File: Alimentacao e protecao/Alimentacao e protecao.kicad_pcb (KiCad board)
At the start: 2 copper layers, 18 parts, among them J1 PinoCheckBateriaVcc, J2 PinoCheckBateriaGND, J3 Conn_01x01_MedidorBateriaVcc, J4 Conn_01x01_MedidorBateriaGnd, Q1 BC548, Q2 BC548, SW1 SW_ON/OFF

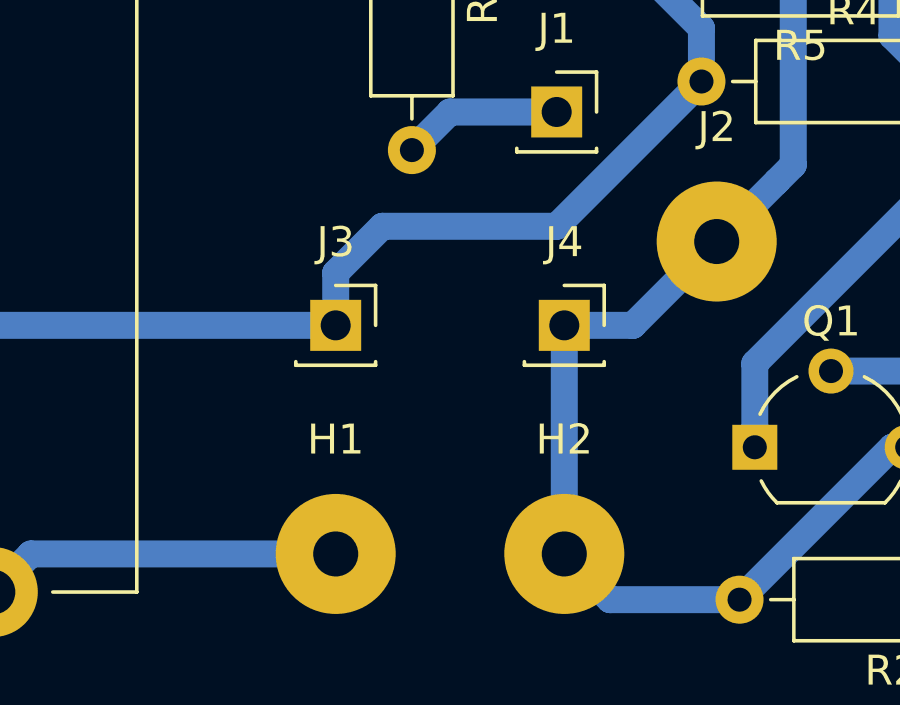
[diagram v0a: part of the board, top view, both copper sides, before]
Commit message: Distribuição dos compenentes praticamente concluída, quase pronta para root.
Placa Central: 5VArduino(pino 15) colocado no pino 16, enquanto o sensorEsq(pino 16) foi colocado no pino 15 para
facilitar o root; Adicionado na placa central os pads de conexao das alimentacoes provenientes do circuito de
alimentacao; Label '5V' substituída por '5VArduino' - decisão a ser revisada; Pads de solda trocados por pads maiores
por questoes de corrente alta (pinos de alimentacao). *Placa de Alimentação: Nome de dois pinos da placa de alimentação
modificados. Pads de solda trocados por pads maiores por questoes de corrente alta (pinos de alimentacao).
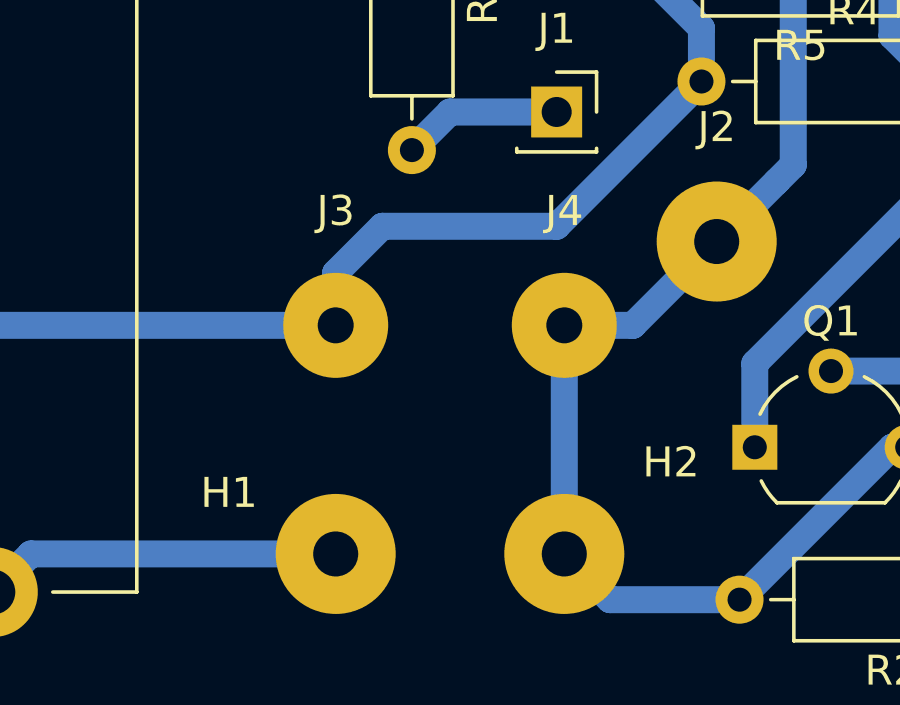
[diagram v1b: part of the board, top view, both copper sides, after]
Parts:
- J3: value Conn_01x01_MedidorBateriaVcc -> 8.4V_PlacaCentral; footprint Connector_PinSocket_2.54mm:PinSocket_1x01_P2.54mm_Vertical -> Connector_Wire:SolderWirePad_1x01_Drill1.2mm
- J4: value Conn_01x01_MedidorBateriaGnd -> GND_PlacaCentral; footprint Connector_PinSocket_2.54mm:PinSocket_1x01_P2.54mm_Vertical -> Connector_Wire:SolderWirePad_1x01_Drill1.2mm
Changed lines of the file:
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@@
       (effects (font (size 1 1) (thickness 0.15)))
     )
-    (fp_text value Fuse-5A (at 13 6 90) (layer F.Fab)
+    (fp_text value Fuse-5A (at 18.034 6 90) (layer F.Fab)
       (effects (font (size 1 1) (thickness 0.15)))
     )
@@
     (tags connector)
     (attr virtual)
-    (fp_text reference H1 (at 0 -3.81) (layer F.SilkS)
+    (fp_text reference H1 (at -3.556 -2.032) (layer F.SilkS)
       (effects (font (size 1 1) (thickness 0.15)))
     )
@@
     (tags connector)
     (attr virtual)
-    (fp_text reference H2 (at 0 -3.81) (layer F.SilkS)
+    (fp_text reference H2 (at 3.556 -3.048) (layer F.SilkS)
       (effects (font (size 1 1) (thickness 0.15)))
     )
@@
       (effects (font (size 1 1) (thickness 0.15)))
     )
-    (fp_text value PinoCheckBateriaGND (at 0 3.81) (layer F.Fab)
+    (fp_text value PinoCheckBateriaGND (at 10.922 -0.508) (layer F.Fab)
       (effects (font (size 1 1) (thickness 0.15)))
     )
@@
     (pad 1 thru_hole circle (at 0 0) (size 4.0005 4.0005) (drill 1.50114) (layers *.Cu *.Mask)
       (net 8 GND))
-  )
-  (module Connector_PinSocket_2.54mm:PinSocket_1x01_P2.54mm_Vertical (layer F.Cu)
-    (at 76.2 90.17)
-    (descr "Through hole straight socket strip, 1x01, 2.54mm pitch, single row (from Kicad 4.0.7), script generated")
-    (tags "Through hole socket strip THT 1x01 2.54mm single row")
-    (fp_text reference J3 (at 0 -2.77) (layer F.SilkS)
-      (effects (font (size 1 1) (thickness 0.15)))
-    )
-    (fp_text value Conn_01x01_MedidorBateriaVcc (at 0 2.77) (layer F.Fab)
-      (effects (font (size 1 1) (thickness 0.15)))
-    )
-    (fp_text user %R (at 0 0) (layer F.Fab)
-      (effects (font (size 1 1) (thickness 0.15)))
-    )
-    (fp_line (start -1.8 1.75) (end -1.8 -1.8) (layer F.CrtYd) (width 0.05))
-    (fp_line (start 1.75 1.75) (end -1.8 1.75) (layer F.CrtYd) (width 0.05))
-    (fp_line (start 1.75 -1.8) (end 1.75 1.75) (layer F.CrtYd) (width 0.05))
-    (fp_line (start -1.8 -1.8) (end 1.75 -1.8) (layer F.CrtYd) (width 0.05))
-    (fp_line (start 0 -1.33) (end 1.33 -1.33) (layer F.SilkS) (width 0.12))
-    (fp_line (start 1.33 -1.33) (end 1.33 0) (layer F.SilkS) (width 0.12))
-    (fp_line (start 1.33 1.21) (end 1.33 1.33) (layer F.SilkS) (width 0.12))
-    (fp_line (start -1.33 1.21) (end -1.33 1.33) (layer F.SilkS) (width 0.12))
-    (fp_line (start -1.33 1.33) (end 1.33 1.33) (layer F.SilkS) (width 0.12))
-    (fp_line (start -1.27 1.27) (end -1.27 -1.27) (layer F.Fab) (width 0.1))
-    (fp_line (start 1.27 1.27) (end -1.27 1.27) (layer F.Fab) (width 0.1))
-    (fp_line (start 1.27 -0.635) (end 1.27 1.27) (layer F.Fab) (width 0.1))
-    (fp_line (start 0.635 -1.27) (end 1.27 -0.635) (layer F.Fab) (width 0.1))
-    (fp_line (start -1.27 -1.27) (end 0.635 -1.27) (layer F.Fab) (width 0.1))
-    (pad 1 thru_hole rect (at 0 0) (size 1.7 1.7) (drill 1) (layers *.Cu *.Mask)
-      (net 3 8.4V))
-    (model ${KISYS3DMOD}/Connector_PinSocket_2.54mm.3dshapes/PinSocket_1x01_P2.54mm_Vertical.wrl
-      (at (xyz 0 0 0))
-      (scale (xyz 1 1 1))
-      (rotate (xyz 0 0 0))
-    )
-  )
-  (module Connector_PinSocket_2.54mm:PinSocket_1x01_P2.54mm_Vertical (layer F.Cu)
-    (at 83.82 90.17)
-    (descr "Through hole straight socket strip, 1x01, 2.54mm pitch, single row (from Kicad 4.0.7), script generated")
-    (tags "Through hole socket strip THT 1x01 2.54mm single row")
-    (fp_text reference J4 (at 0 -2.77) (layer F.SilkS)
-      (effects (font (size 1 1) (thickness 0.15)))
-    )
-    (fp_text value Conn_01x01_MedidorBateriaGnd (at 0 2.77) (layer F.Fab)
-      (effects (font (size 1 1) (thickness 0.15)))
-    )
-    (fp_line (start -1.27 -1.27) (end 0.635 -1.27) (layer F.Fab) (width 0.1))
-    (fp_line (start 0.635 -1.27) (end 1.27 -0.635) (layer F.Fab) (width 0.1))
-    (fp_line (start 1.27 -0.635) (end 1.27 1.27) (layer F.Fab) (width 0.1))
-    (fp_line (start 1.27 1.27) (end -1.27 1.27) (layer F.Fab) (width 0.1))
-    (fp_line (start -1.27 1.27) (end -1.27 -1.27) (layer F.Fab) (width 0.1))
-    (fp_line (start -1.33 1.33) (end 1.33 1.33) (layer F.SilkS) (width 0.12))
-    (fp_line (start -1.33 1.21) (end -1.33 1.33) (layer F.SilkS) (width 0.12))
-    (fp_line (start 1.33 1.21) (end 1.33 1.33) (layer F.SilkS) (width 0.12))
-    (fp_line (start 1.33 -1.33) (end 1.33 0) (layer F.SilkS) (width 0.12))
-    (fp_line (start 0 -1.33) (end 1.33 -1.33) (layer F.SilkS) (width 0.12))
-    (fp_line (start -1.8 -1.8) (end 1.75 -1.8) (layer F.CrtYd) (width 0.05))
-    (fp_line (start 1.75 -1.8) (end 1.75 1.75) (layer F.CrtYd) (width 0.05))
-    (fp_line (start 1.75 1.75) (end -1.8 1.75) (layer F.CrtYd) (width 0.05))
-    (fp_line (start -1.8 1.75) (end -1.8 -1.8) (layer F.CrtYd) (width 0.05))
-    (fp_text user %R (at 0 0) (layer F.Fab)
-      (effects (font (size 1 1) (thickness 0.15)))
-    )
-    (pad 1 thru_hole rect (at 0 0) (size 1.7 1.7) (drill 1) (layers *.Cu *.Mask)
-      (net 8 GND))
-    (model ${KISYS3DMOD}/Connector_PinSocket_2.54mm.3dshapes/PinSocket_1x01_P2.54mm_Vertical.wrl
-      (at (xyz 0 0 0))
-      (scale (xyz 1 1 1))
-      (rotate (xyz 0 0 0))
-    )
   )
   (module Package_TO_SOT_THT:TO-92_Wide (layer F.Cu)
@@
       (effects (font (size 1 1) (thickness 0.15)))
     )
-    (fp_text value R6K6MedidorDeBateria (at 5.08 2.37 180) (layer F.Fab)
+    (fp_text value R6K6MedidorDeBateria (at -7.874 -3.302 180) (layer F.Fab)
       (effects (font (size 1 1) (thickness 0.15)))
     )
@@
       (effects (font (size 1 1) (thickness 0.15)))
     )
-    (fp_text value R1KMedidorDeBateria (at 5.08 2.37 90) (layer F.Fab)
+    (fp_text value R1KMedidorDeBateria (at 0.254 12.7 180) (layer F.Fab)
       (effects (font (size 1 1) (thickness 0.15)))
     )
@@
       (effects (font (size 1 1) (thickness 0.15)))
     )
-    (fp_text value SW_ON/OFF (at 0 -0.5 90) (layer F.Fab)
+    (fp_text value SW_ON/OFF (at 0.762 -6.858 90) (layer F.Fab)
       (effects (font (size 1 1) (thickness 0.15)))
     )
@@
       (net 3 8.4V))
   )
+  (module Connector_Wire:SolderWirePad_1x01_Drill1.2mm (layer F.Cu)
+    (at 76.2 90.17)
+    (descr "Wire solder connection")
+    (tags connector)
+    (attr virtual)
+    (fp_text reference J3 (at 0 -3.81) (layer F.SilkS)
+      (effects (font (size 1 1) (thickness 0.15)))
+    )
+    (fp_text value 8.4V_PlacaCentral (at 0 3.175) (layer F.Fab)
+      (effects (font (size 1 1) (thickness 0.15)))
+    )
+    (fp_text user %R (at 0 0) (layer F.Fab)
+      (effects (font (size 1 1) (thickness 0.15)))
+    )
+    (fp_line (start -2.25 -2.25) (end 2.25 -2.25) (layer F.CrtYd) (width 0.05))
+    (fp_line (start -2.25 -2.25) (end -2.25 2.25) (layer F.CrtYd) (width 0.05))
+    (fp_line (start 2.25 2.25) (end 2.25 -2.25) (layer F.CrtYd) (width 0.05))
+    (fp_line (start 2.25 2.25) (end -2.25 2.25) (layer F.CrtYd) (width 0.05))
+    (pad 1 thru_hole circle (at 0 0) (size 3.50012 3.50012) (drill 1.19888) (layers *.Cu *.Mask)
+      (net 3 8.4V))
+  )
+  (module Connector_Wire:SolderWirePad_1x01_Drill1.2mm (layer F.Cu)
+    (at 83.82 90.17)
+    (descr "Wire solder connection")
+    (tags connector)
+    (attr virtual)
+    (fp_text reference J4 (at 0 -3.81) (layer F.SilkS)
+      (effects (font (size 1 1) (thickness 0.15)))
+    )
+    (fp_text value GND_PlacaCentral (at 0 3.175) (layer F.Fab)
+      (effects (font (size 1 1) (thickness 0.15)))
+    )
+    (fp_line (start 2.25 2.25) (end -2.25 2.25) (layer F.CrtYd) (width 0.05))
+    (fp_line (start 2.25 2.25) (end 2.25 -2.25) (layer F.CrtYd) (width 0.05))
+    (fp_line (start -2.25 -2.25) (end -2.25 2.25) (layer F.CrtYd) (width 0.05))
+    (fp_line (start -2.25 -2.25) (end 2.25 -2.25) (layer F.CrtYd) (width 0.05))
+    (fp_text user %R (at 0 0) (layer F.Fab)
+      (effects (font (size 1 1) (thickness 0.15)))
+    )
+    (pad 1 thru_hole circle (at 0 0) (size 3.50012 3.50012) (drill 1.19888) (layers *.Cu *.Mask)
+      (net 8 GND))
+  )
   (gr_line (start 103.124 101.6) (end 103.124 66.548) (layer B.Paste) (width 0.2))

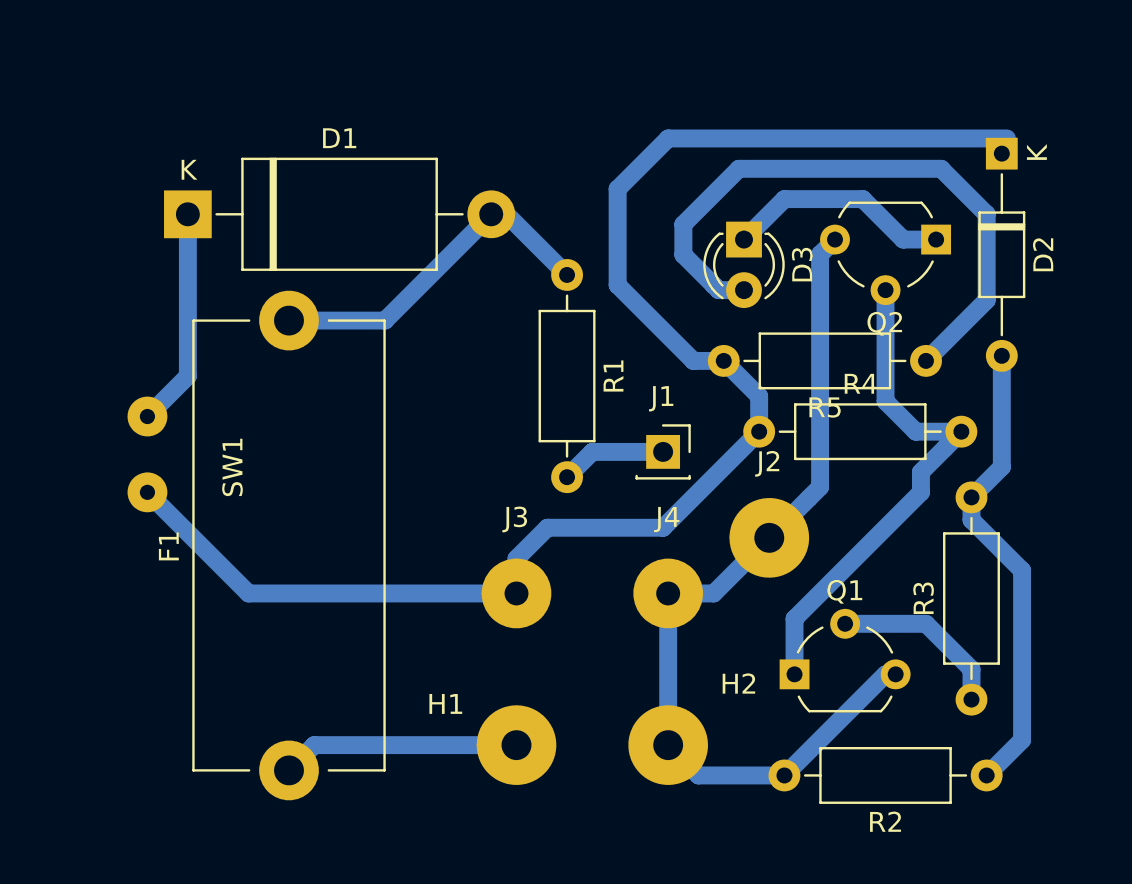
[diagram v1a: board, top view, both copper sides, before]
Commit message: Placa de alimentação finalizada e pronta para manunfatura
Foram colocados textos indicadores próximos a pinos de destaque
Os pinos de conexão da bateria estão indicados com + e -
Os pinos a serem conectados na PC(Placa central) estão indicados com os símbolos pc+ e pc-
Foi reservada uma área para ser colocado o botão, indicada por texto
Foram adicionados também furos para parafusos
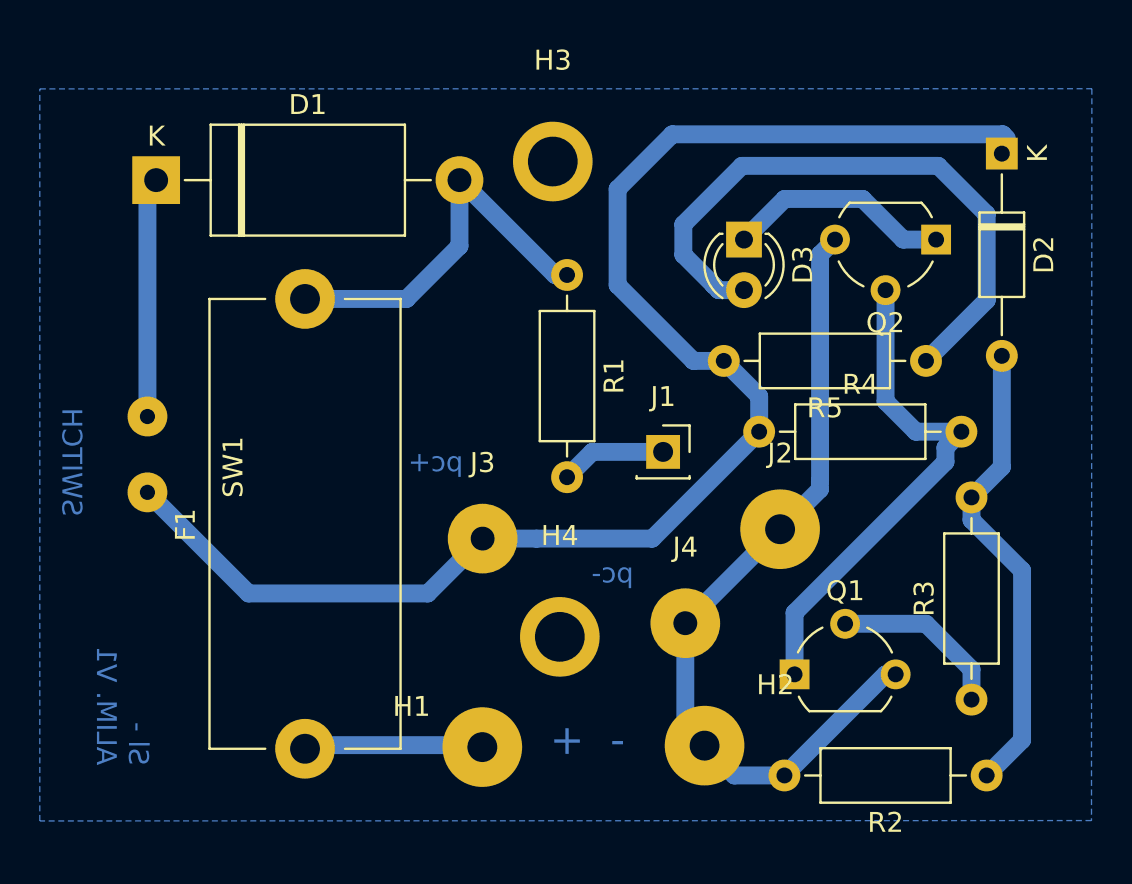
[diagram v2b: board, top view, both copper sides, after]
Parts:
- added H3: Furos, Wire_Pads:SolderWirePad_single_2-5mmDrill, F.Cu at (78.0, 68.5)
- added H4: Furos, Wire_Pads:SolderWirePad_single_2-5mmDrill, F.Cu at (78.4, 92.3)
- moved J3 3.24 mm to (74.5, 87.4)
- moved D1 2.34 mm to (58.1, 69.4)
- moved H2 1.83 mm to (85.6, 97.8)
- moved J4 1.72 mm to (84.7, 91.7)
- moved H1 1.72 mm to (74.5, 97.9)
- moved F1 1.35 mm to (65.6, 98.0)
- moved J2 0.70 mm to (89.4, 86.9)
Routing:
- net Net-(F1-Pad1): track 12.0 -> 9.02 mm
- net GND: track 44.4 -> 41.7 mm
- net Net-(D1-Pad2): track 17.4 -> 19.6 mm
- net Net-(D1-Pad1): track 11.0 -> 12.1 mm
- net 8.4V: track 73.9 -> 73.0 mm
- added copper zone on B.Cu, net GND
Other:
- net class Default: clearance 0.2 -> 0.6
- rule trace_clearance: 0.2 -> 0.6
- rule trace_min: 0.2 -> 0.9
- board text added: "+"
- board text added: "-"
- board text added: "SWITCH"
- board text added: "Sl - ALIM. V1"
- board text added: "pc+"
- board text added: "pc-"
